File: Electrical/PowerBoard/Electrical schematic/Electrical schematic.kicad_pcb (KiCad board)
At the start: 2 copper layers, 8.6 x 4.4 mm, 24 parts, among them J1 S4B-XH-SM4-TB, J2 XT60PW-M, J3 XT60PW-M, J4 2171750001, J5 XT60PW-M, U1 LMZ22005TZ/NOPB, U2 ACS715LLCTR-30A-T, U3 TLV2370IDBVR, U4 TMUX1204DGSR

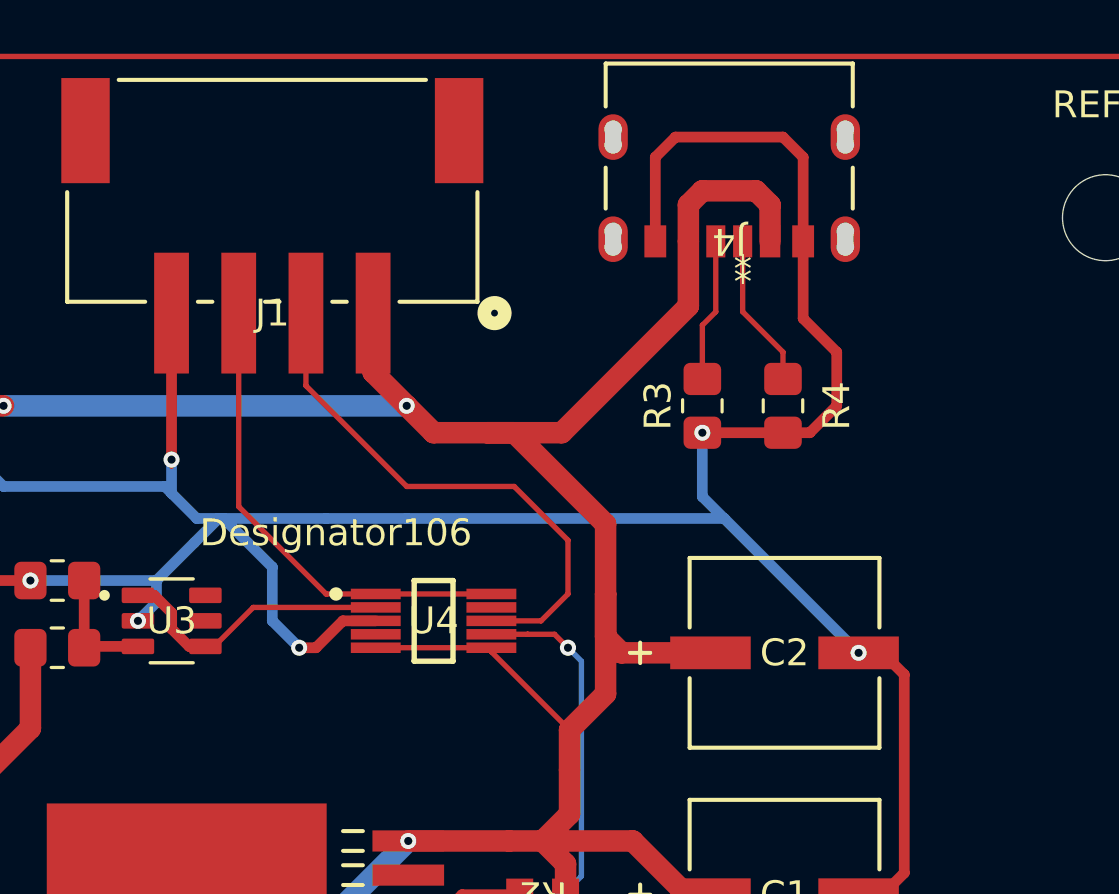
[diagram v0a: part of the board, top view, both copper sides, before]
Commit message: new mux/usbA
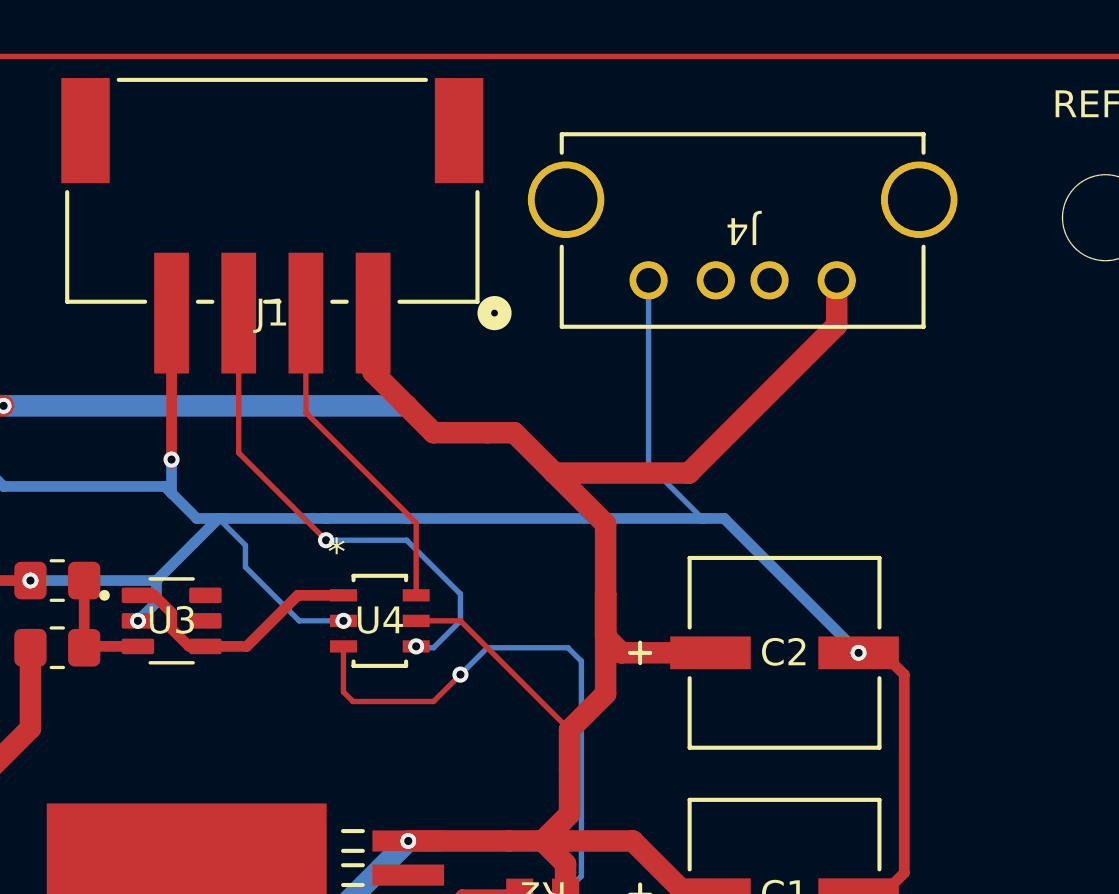
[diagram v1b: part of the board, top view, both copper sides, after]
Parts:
- removed R3, R4: 5.1k, Resistor_SMD:R_0805_2012Metric_Pad1.20x1.40mm_HandSolder
- C1, C2, C3: footprint footprints 3:PCAP_SVP_C6_PAN -> _Footprints:PCAP_SVP_C6_PAN
- J4: value 2171750001 -> USB-A1VSB6; footprint _Footprints:2171750001_MOL -> _Footprints:CONN4_USB-A1VSB6_OST
- R1, R2: footprint footprints 6:RC0805N_PAN -> _Footprints:RC0805N_PAN
- U1: footprint footprints 8:TZA07A -> _Footprints:TZA07A
- U4: value TMUX1204DGSR -> 74LVC1G157GV_125; footprint _Footprints:DGS0010A-IPC_A -> _Footprints:TSOP6_SOT457_NEX
- moved J4 6.01 mm to (163.0, 86.3)
- moved U4 2.00 mm to (146.0, 99.0)
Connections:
- J1 pad 2: Net-(U4-D) -> Net-(U4-S)
- J1 pad 3: Net-(U4-A0) -> Net-(U4-Y)
- U4 pad 1: Net-(U4-A0) -> /Voltage Reading/OUT
- U4 pad 2: /Voltage Reading/OUT -> GND
- U4 pad 3: GND -> /Current Sensor/VOLTAGE OUT (of reading)
- U4 pad 4: unconnected-(U4-S3-Pad4) -> Net-(U4-Y)
- U4 pad 6: /Buck Converter/Vout (5V 5A) -> Net-(U4-S)
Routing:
- net GND: track 224.6 -> 203.7 mm, vias 9 -> 8
- net Net-(U4-D): track 20.1 -> 0.00 mm
- net Net-(U4-Y): track 0.00 -> 18.7 mm, vias 0 -> 2
- net Net-(U4-A0): track 17.9 -> 0.00 mm
- net Net-(U4-S): track 0.00 -> 12.2 mm
- net /Current Sensor/VOLTAGE OUT (of reading): track 33.2 -> 41.2 mm
- net Net-(J4-CC1): track 5.74 -> 0.00 mm
- net Net-(J4-CC2): track 5.33 -> 0.00 mm
- net /Buck Converter/Vout (5V 5A): track 124.0 -> 119.2 mm, vias 4 -> 3
- net /Voltage Reading/OUT: track 10.6 -> 9.57 mm
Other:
- board outline removed

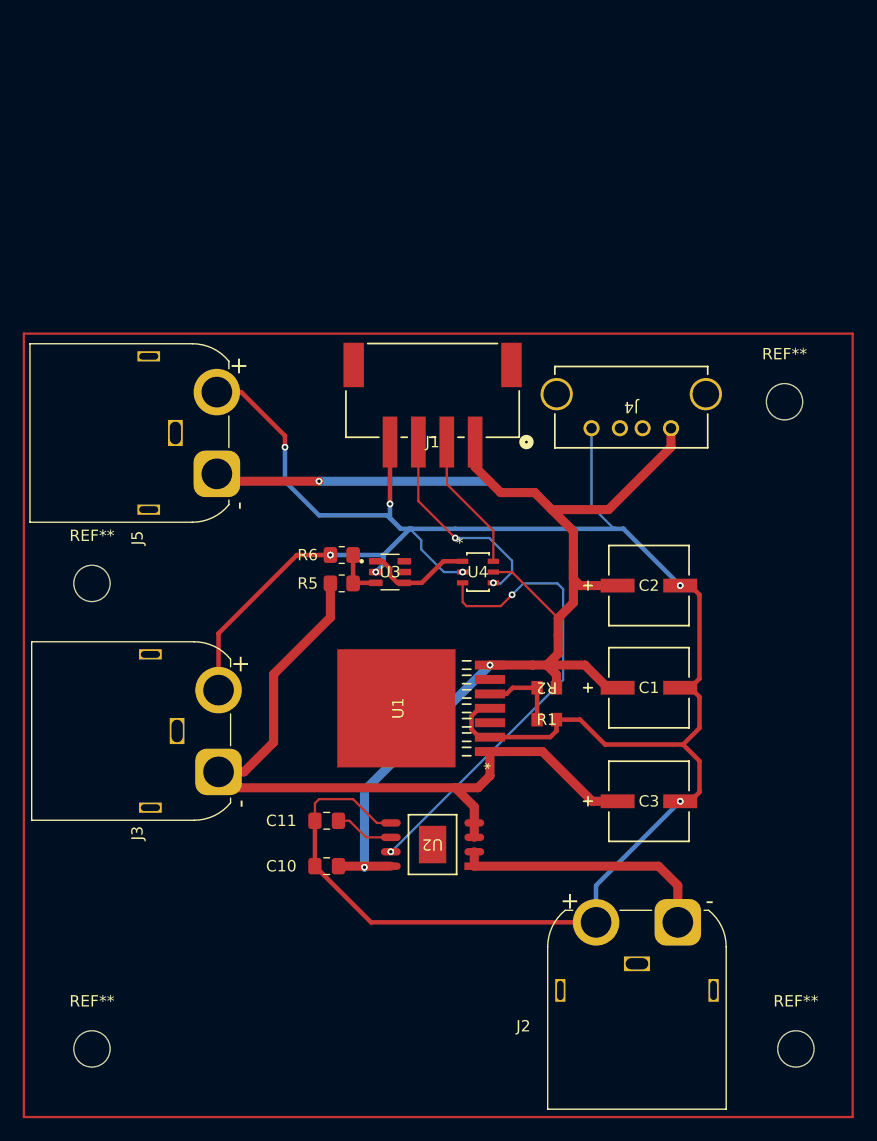
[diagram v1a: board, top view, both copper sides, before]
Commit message: rewiring to be smaller/new mux/ fixing xt60
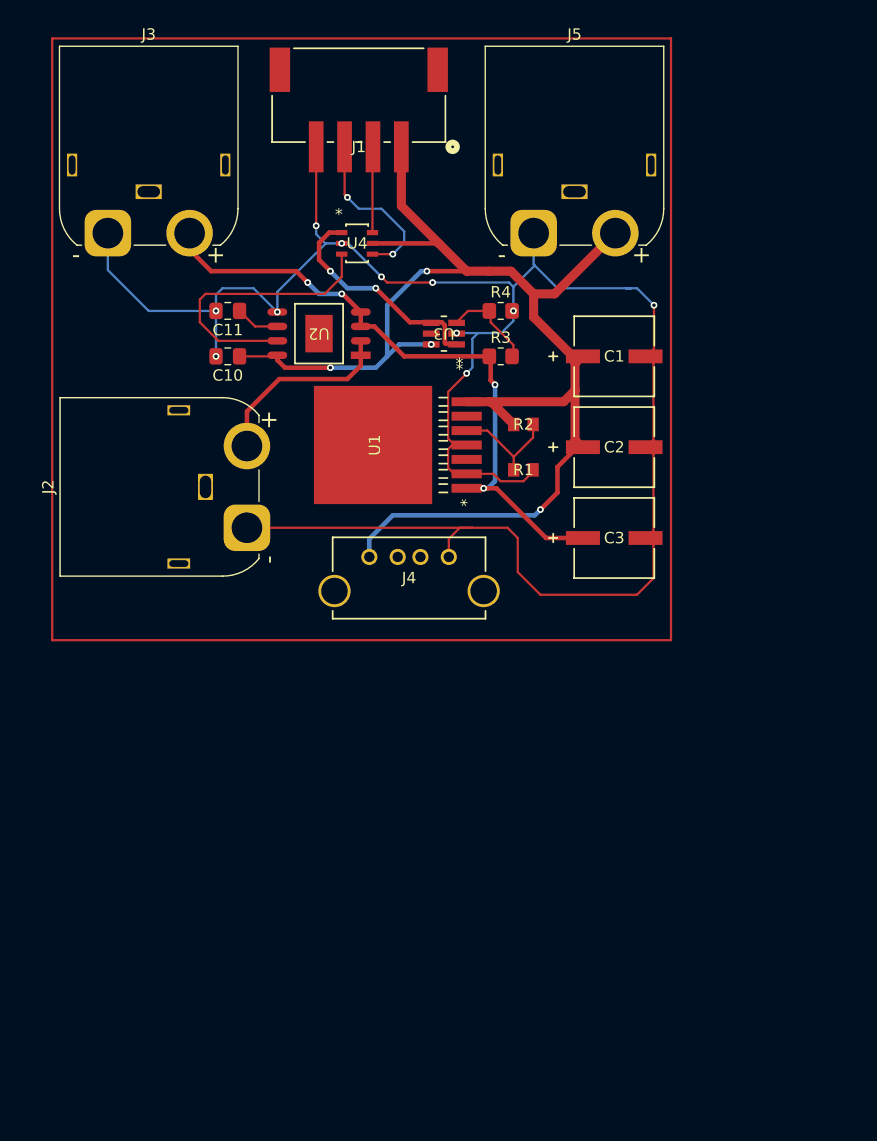
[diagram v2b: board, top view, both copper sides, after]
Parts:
- removed R5: 1M, Resistor_SMD:R_0805_2012Metric_Pad1.20x1.40mm_HandSolder
- removed R6: 0.333M, Resistor_SMD:R_0805_2012Metric_Pad1.20x1.40mm_HandSolder
- removed REF** (x4): MountingHole_3.2mm_M3, MountingHole:MountingHole_3.2mm_M3
- added R3: 1M, Resistor_SMD:R_0805_2012Metric_Pad1.20x1.40mm_HandSolder, F.Cu at (148.0, 80.0)
- added R4: 0.333M, Resistor_SMD:R_0805_2012Metric_Pad1.20x1.40mm_HandSolder, F.Cu at (148.0, 76.0)
- U3: footprint TLV2370IDBVR:SOT95P280X145-6N -> _Footprints:DBV6
- moved J2 51.5 mm to (125.7, 95.1), turned to 90 degrees
- moved J3 48.4 mm to (113.4, 69.2), turned to 0 degrees
- moved U2 46.1 mm to (132.0, 78.0)
- moved C10 45.7 mm to (124.0, 80.0)
- moved C11 45.7 mm to (124.0, 76.0)
- moved J5 35.0 mm to (150.9, 69.2), turned to 0 degrees
- moved U4 30.8 mm to (135.4, 70.0)
- moved C1 29.3 mm to (158.0, 80.0)
- moved J4 28.9 mm to (136.4, 97.7), turned to 0 degrees
- moved J1 26.8 mm to (135.5, 57.0)
- moved C3 23.4 mm to (158.0, 96.0)
- moved R2 23.3 mm to (150.0, 86.0), turned to 0 degrees
- moved U1 23.3 mm to (136.9, 87.8)
- moved R1 22.1 mm to (150.0, 90.0)
- moved U3 21.5 mm to (143.0, 78.0), turned to 180 degrees
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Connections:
- net /Voltage Reading/OUT renamed Net-(U3-IN-)
- J2 pad 1: /Current Sensor/CURRENT IN -> GND
- J2 pad 2: GND -> /Current Sensor/CURRENT IN
- J3 pad 1: /Buck Converter/Vin (12V) -> GND
- J3 pad 2: GND -> /Buck Converter/Vin (12V)
- J5 pad 1: /Buck Converter/Vout (5V 5A) -> GND
- J5 pad 2: GND -> /Buck Converter/Vout (5V 5A)
- U3 pad 6: +5V -> /Buck Converter/Vout (5V 5A)
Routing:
- net GND: track 203.7 -> 182.8 mm, vias 8 -> 11
- net /Current Sensor/VOLTAGE OUT (of reading): track 41.2 -> 24.8 mm, vias 2 -> 0
- net Net-(U3-IN-): track 9.57 -> 20.0 mm, vias 0 -> 2
- net /Buck Converter/Vin (12V): track 67.2 -> 57.1 mm, vias 0 -> 4
- net /Current Sensor/CURRENT IN: track 23.1 -> 16.9 mm
- net Net-(U4-S): track 12.2 -> 7.57 mm
- net /Buck Converter/Vout (5V 5A): track 119.2 -> 123.5 mm, vias 3 -> 4
- net Net-(U3-IN+): track 4.52 -> 8.24 mm
- net Net-(U4-Y): track 18.7 -> 15.0 mm
- net Net-(U1-FB): track 7.18 -> 9.81 mm
- net Net-(U2-FILTER): track 5.22 -> 3.89 mm

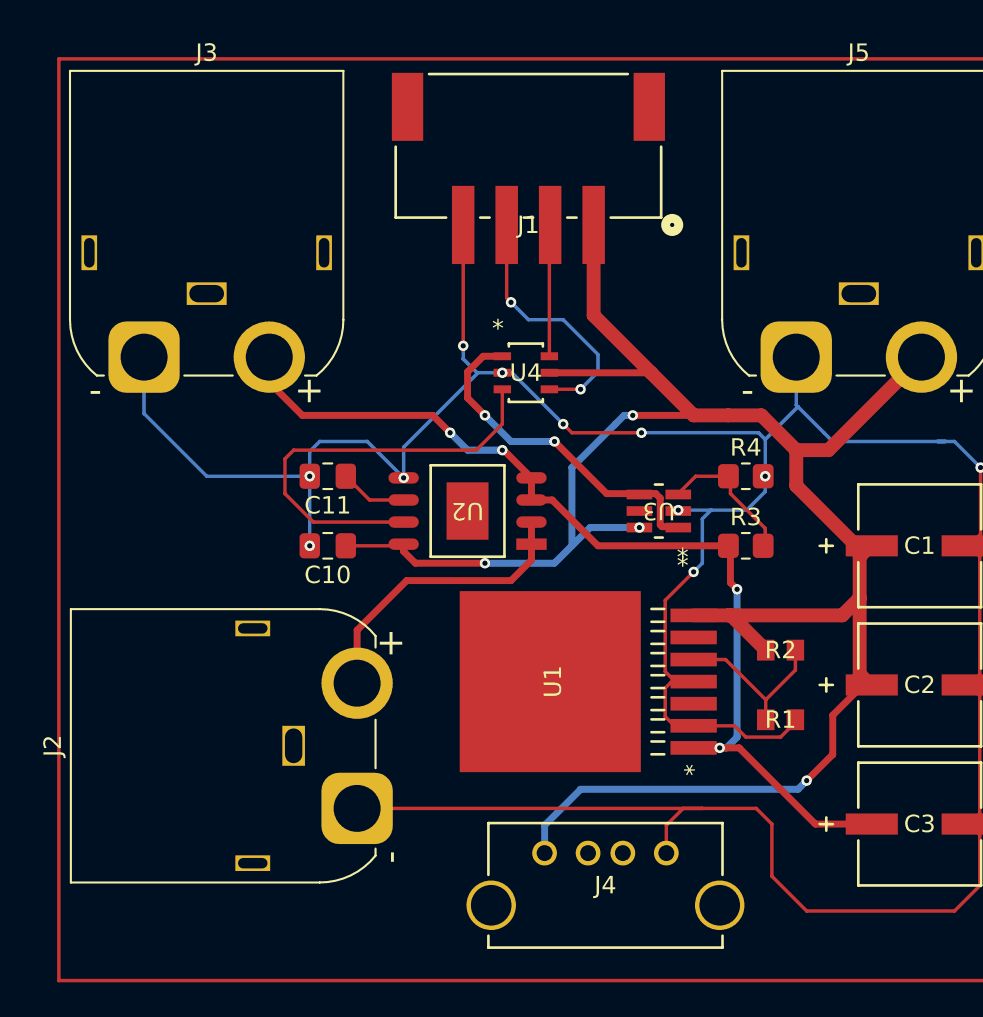
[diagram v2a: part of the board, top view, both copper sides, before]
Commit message: Edited silkscreen labels, moved USB port to edge
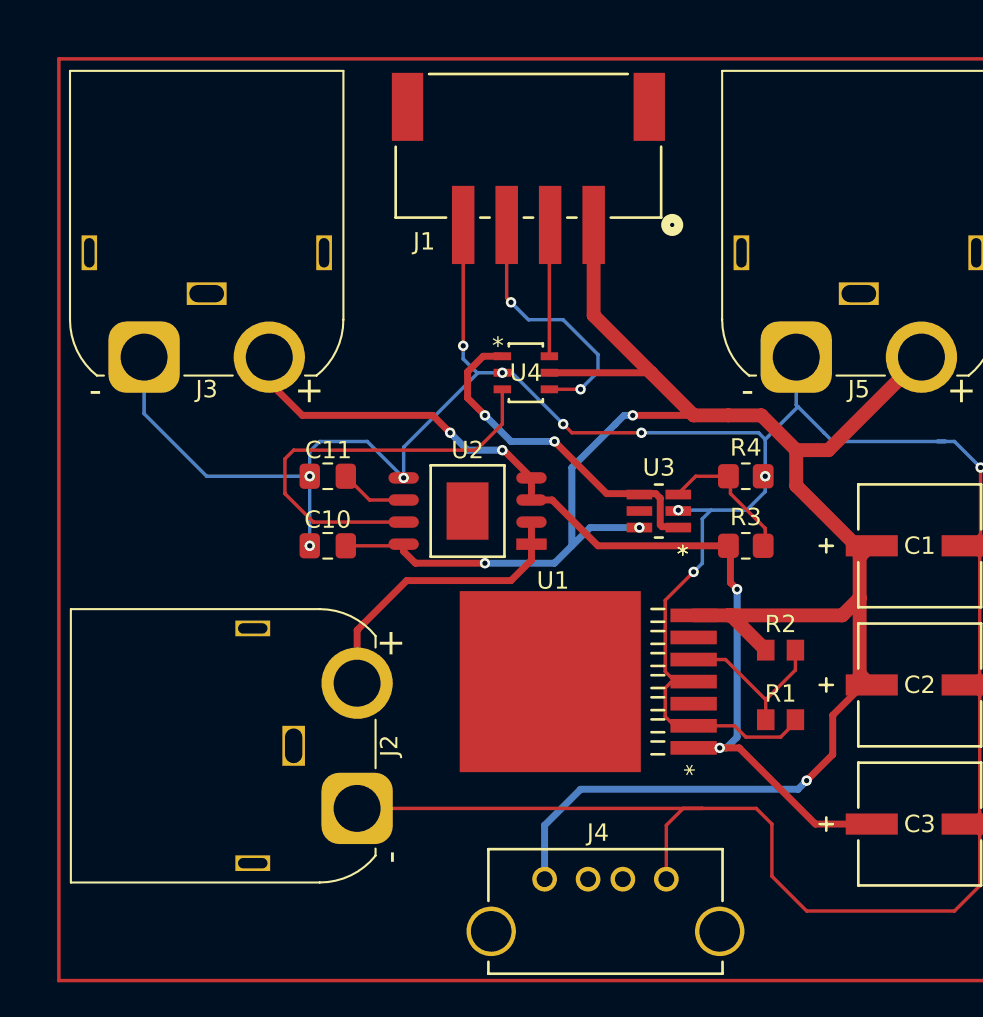
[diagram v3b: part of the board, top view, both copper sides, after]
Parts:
- moved J4 1.50 mm to (136.4, 99.2)
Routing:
- net GND: track 182.8 -> 184.3 mm
- net /Buck Converter/Vout (5V 5A): track 123.5 -> 125.0 mm
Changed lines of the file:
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@@
 		(tags "ERJ-6ENF5621V ")
 		(property "Reference" "R1"
-			(at 0 0 0)
+			(at 0 -1.5 0)
 			(unlocked yes)
 			(layer "F.SilkS")
@@
 		(tags "ACS715LLCTR-30A-T ")
 		(property "Reference" "U2"
-			(at 0 0 180)
+			(at 0 3.5 0)
 			(unlocked yes)
 			(layer "F.SilkS")
@@
 	(footprint "_Footprints:CONN4_USB-A1VSB6_OST"
 		(layer "F.Cu")
-		(at 136.430001 97.669349)
+		(at 136.430001 99.169349)
 		(tags "USB-A1VSB6 ")
 		(property "Reference" "J4"
-			(at 3.499999 1.850001 0)
+			(at 3.069999 -2.669349 0)
 			(unlocked yes)
 			(layer "F.SilkS")
@@
 		(tags "ERJ-6ENF5621V ")
 		(property "Reference" "R2"
-			(at 0 0 0)
+			(at 0 -1.5 0)
 			(unlocked yes)
 			(layer "F.SilkS")
@@
 		)
 		(fp_text user "*"
-			(at -1.60655 -2.5502 0)
+			(at -1.60655 -1.549999 0)
 			(layer "F.SilkS")
 			(effects
@@
 		)
 		(fp_text user "*"
-			(at -1.60655 -2.5502 0)
+			(at -1.60655 -1.549999 0)
 			(unlocked yes)
 			(layer "F.SilkS")
@@
 		(tags "S4B-XH-SM4-TB ")
 		(property "Reference" "J1"
-			(at 0 4.549501 0)
+			(at -6 5.5 0)
 			(unlocked yes)
 			(layer "F.SilkS")
@@
 		(tags "RC Connector XT60")
 		(property "Reference" "J3"
-			(at 3.6 -17.5 360)
+			(at 3.6 1.85 0)
 			(layer "F.SilkS")
 			(effects
@@
 		)
 		(property "Value" "XT60PW-M"
-			(at 3.6 4 360)
+			(at 3.6 4 0)
 			(layer "F.Fab")
 			(effects
@@
 		)
 		(fp_text user "+"
-			(at 9.5 1.9 360)
+			(at 9.5 1.9 0)
 			(layer "F.SilkS")
 			(effects
@@
 		)
 		(fp_text user "-"
-			(at -2.8 1.9 360)
+			(at -2.8 1.9 0)
 			(layer "F.SilkS")
 			(effects
@@
 		)
 		(fp_text user "${REFERENCE}"
-			(at 3.6 -11 360)
+			(at 3.6 -11 0)
 			(layer "F.Fab")
 			(effects
@@
 		(tags "RC Connector XT60")
 		(property "Reference" "J5"
-			(at 3.6 -17.5 0)
+			(at 3.6 1.85 0)
 			(layer "F.SilkS")
 			(effects
@@
 		(tags "capacitor handsolder")
 		(property "Reference" "C11"
-			(at 0 -1.68 0)
+			(at -0.0375 1.5 0)
 			(layer "F.SilkS")
 			(effects
@@
 		(tags "TLV2370IDBVR ")
 		(property "Reference" "U3"
-			(at 0 0 180)
+			(at 0 2.5 0)
 			(unlocked yes)
 			(layer "F.SilkS")
@@
 		)
 		(property "Footprint" "DBV6"
-			(at 0 0 360)
+			(at 0 0 0)
 			(layer "F.Fab")
 			(hide yes)
@@
 		)
 		(property "Datasheet" "TLV2370IDBVR"
-			(at 0 0 360)
+			(at 0 0 0)
 			(layer "F.Fab")
 			(hide yes)
@@
 		)
 		(property "Description" ""
-			(at 0 0 360)
+			(at 0 0 0)
 			(layer "F.Fab")
 			(hide yes)
@@
 		)
 		(fp_text user "*"
-			(at -1.3716 -2.6518 360)
+			(at -1.3716 -2.5 0)
 			(layer "F.SilkS")
 			(effects
@@
 		)
 		(fp_text user "*"
-			(at -1.3716 -2.6518 180)
+			(at -1.3716 -2 180)
 			(unlocked yes)
 			(layer "F.SilkS")
@@
 		)
 		(fp_text user "*"
-			(at -1.3716 -2.6518 360)
+			(at -1.3716 -2.6518 0)
 			(layer "F.Fab")
 			(effects
@@
 		(tags "capacitor handsolder")
 		(property "Reference" "C10"
-			(at 0 -1.68 0)
+			(at 0 1.5 0)
 			(layer "F.SilkS")
 			(effects
@@
 		(tags "LMZ22005TZ/NOPB ")
 		(property "Reference" "U1"
-			(at 0 0 90)
+			(at 5.81 0 0)
 			(unlocked yes)
 			(layer "F.SilkS")
@@
 		(tags "RC Connector XT60")
 		(property "Reference" "J2"
-			(at 3.6 -17.5 90)
+			(at 3.6 1.85 90)
 			(layer "F.SilkS")
 			(effects
@@
 	)
 	(segment
+		(start 143.429999 96.070001)
+		(end 143.429999 99.169349)
+		(width 0.2)
+		(layer "F.Cu")
+		(net 1)
+	)
+	(segment
 		(start 161.4528 95.381022)
 		(end 161.4528 88.618978)
@@
 	)
 	(segment
-		(start 143.429999 96.070001)
-		(end 144.4 95.1)
-		(width 0.2)
-		(layer "F.Cu")
-		(net 1)
-	)
-	(segment
 		(start 161.4528 88.618978)
 		(end 160.833822 88)
@@
 	)
 	(segment
-		(start 144.4 95.1)
-		(end 145.5 95.1)
+		(start 143.9428 87.81)
+		(end 143.3665 87.2337)
 		(width 0.2)
 		(layer "F.Cu")
@@
 	)
 	(segment
-		(start 143.9428 87.81)
-		(end 143.3665 87.2337)
+		(start 145.5 95.1)
+		(end 144.4 95.1)
 		(width 0.2)
 		(layer "F.Cu")
@@
 	)
 	(segment
+		(start 144.4 95.1)
+		(end 143.429999 96.070001)
+		(width 0.2)
+		(layer "F.Cu")
+		(net 1)
+	)
+	(segment
 		(start 148.6 95.1)
 		(end 149.5 96)
@@
 	)
 	(segment
-		(start 143.429999 96.070001)
-		(end 143.429999 97.669349)
-		(width 0.2)
-		(layer "F.Cu")
-		(net 1)
-	)
-	(segment
 		(start 147.35 90.35)
 		(end 148 91)
@@
 	)
 	(segment
-		(start 138 80)
-		(end 139.049999 78.950001)
+		(start 151.5 93.5)
+		(end 151 94)
 		(width 0.4)
 		(layer "B.Cu")
@@
 	)
 	(segment
-		(start 138.5 94)
-		(end 136.430001 96.069999)
+		(start 138 80)
+		(end 139.049999 78.950001)
 		(width 0.4)
 		(layer "B.Cu")
@@
 	)
 	(segment
-		(start 151 94)
-		(end 138.5 94)
+		(start 141 72.5)
+		(end 141.5 72.5)
 		(width 0.4)
 		(layer "B.Cu")
@@
 	)
 	(segment
-		(start 141 72.5)
-		(end 141.5 72.5)
+		(start 139.049999 78.950001)
+		(end 141.8824 78.950001)
 		(width 0.4)
 		(layer "B.Cu")
@@
 	)
 	(segment
-		(start 139.049999 78.950001)
-		(end 141.8824 78.950001)
+		(start 138.5 94)
+		(end 136.430001 96.069999)
 		(width 0.4)
 		(layer "B.Cu")
@@
 	)
 	(segment
-		(start 133 81)
-		(end 137 81)
+		(start 151 94)
+		(end 138.5 94)
 		(width 0.4)
 		(layer "B.Cu")
@@
 	)
 	(segment
-		(start 136.430001 96.069999)
-		(end 136.430001 97.669349)
+		(start 133 81)
+		(end 137 81)
 		(width 0.4)
 		(layer "B.Cu")
@@
 	)
 	(segment
-		(start 151.5 93.5)
-		(end 151 94)
+		(start 136.430001 96.069999)
+		(end 136.430001 99.169349)
 		(width 0.4)
 		(layer "B.Cu")
